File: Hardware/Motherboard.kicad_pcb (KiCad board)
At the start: 2 copper layers, 12 parts, among them J1 Conn_01x07_Male, U1 PIC18F23K22, U2 DS3231M, U3 Adafruit_BME680

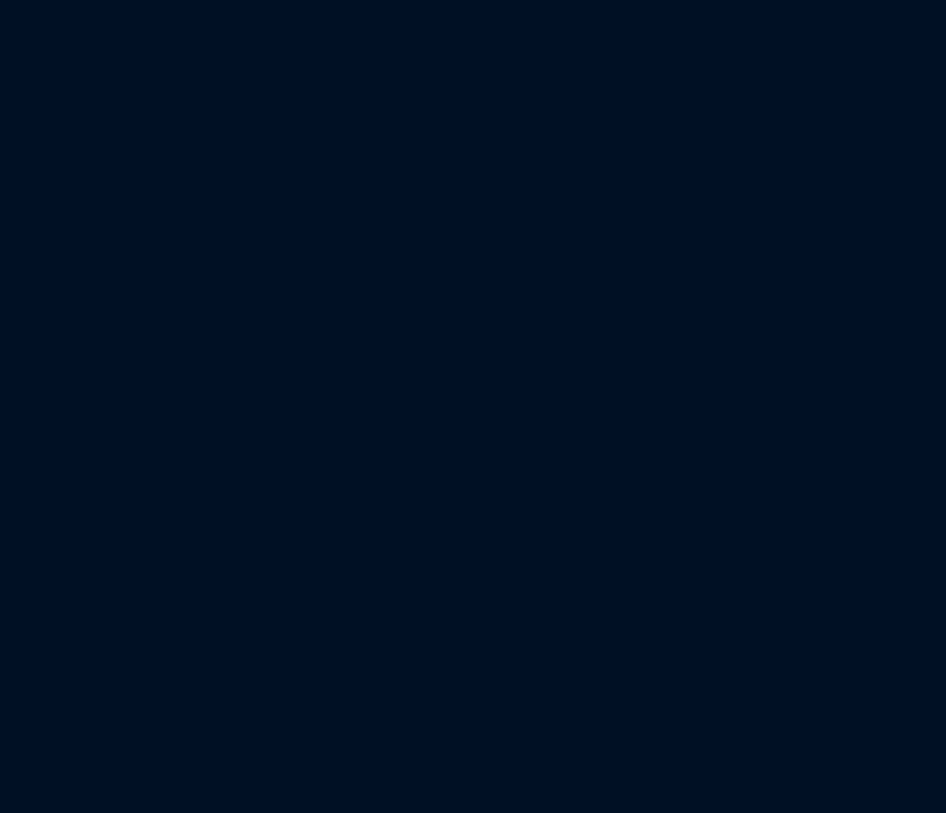
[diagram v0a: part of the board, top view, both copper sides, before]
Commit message: [Hardware] Replaced PIC18F26K22 microcontroller by PIC18F46K22 to have more pins.
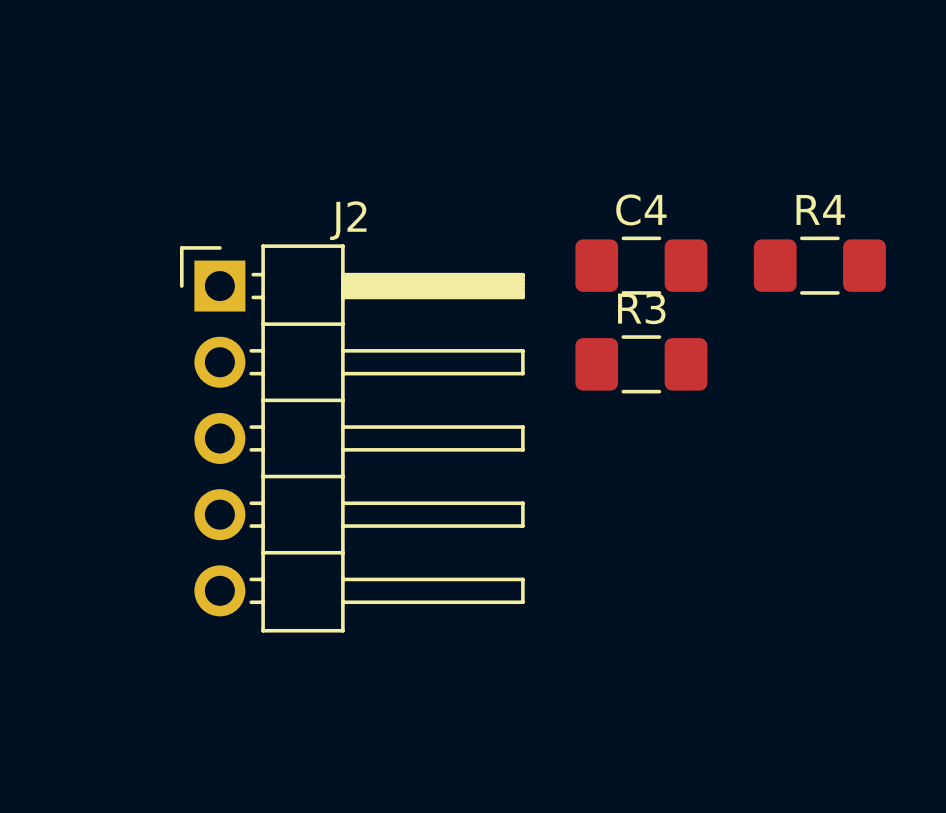
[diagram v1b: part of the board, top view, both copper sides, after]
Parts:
- added C4: 100n, Capacitor_SMD:C_1206_3216Metric_Pad1.42x1.75mm_HandSolder, F.Cu at (190.8, 23.4)
- added J2: Conn_01x05_Male, Connector_PinHeader_2.54mm:PinHeader_1x05_P2.54mm_Horizontal, F.Cu at (176.7, 24.0)
- added R3: 10K, Resistor_SMD:R_1206_3216Metric_Pad1.42x1.75mm_HandSolder, F.Cu at (190.8, 26.7)
- added R4: 220, Resistor_SMD:R_1206_3216Metric_Pad1.42x1.75mm_HandSolder, F.Cu at (196.7, 23.4)

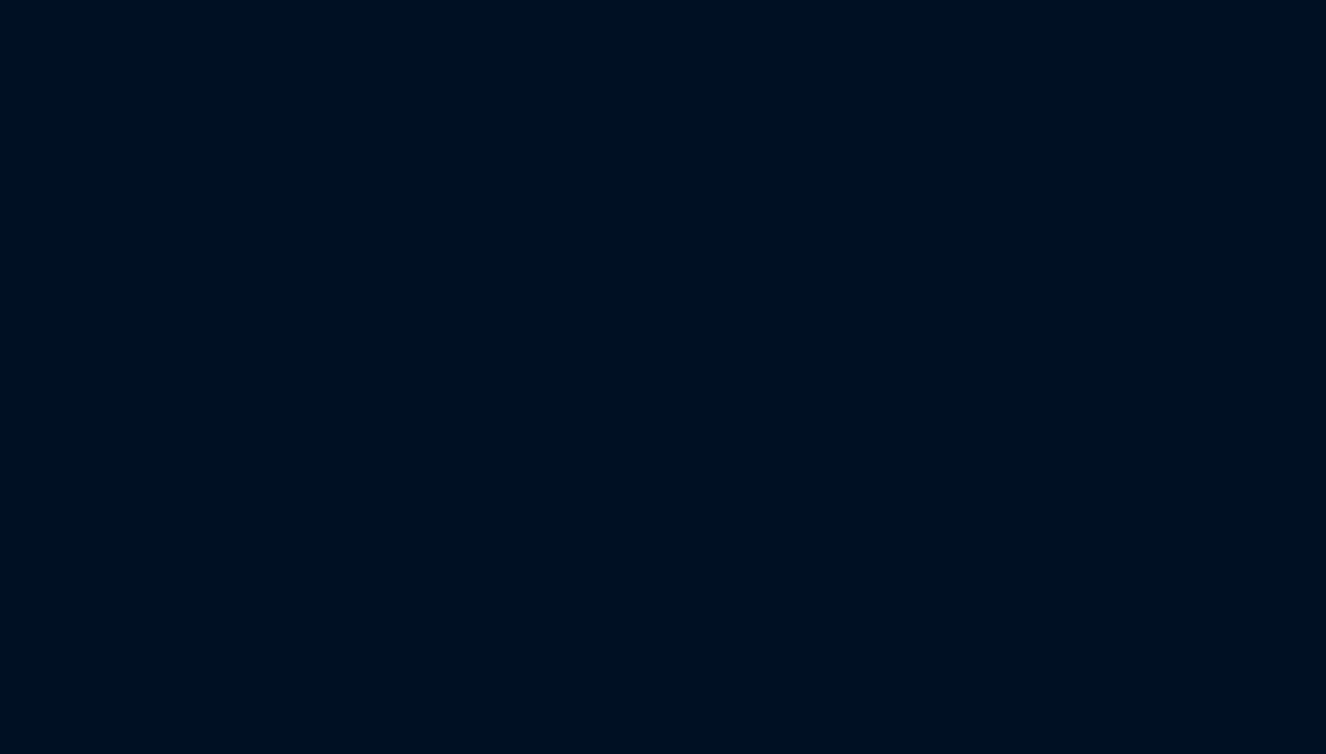
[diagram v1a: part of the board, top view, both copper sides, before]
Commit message: [Hardware] Added buttons.
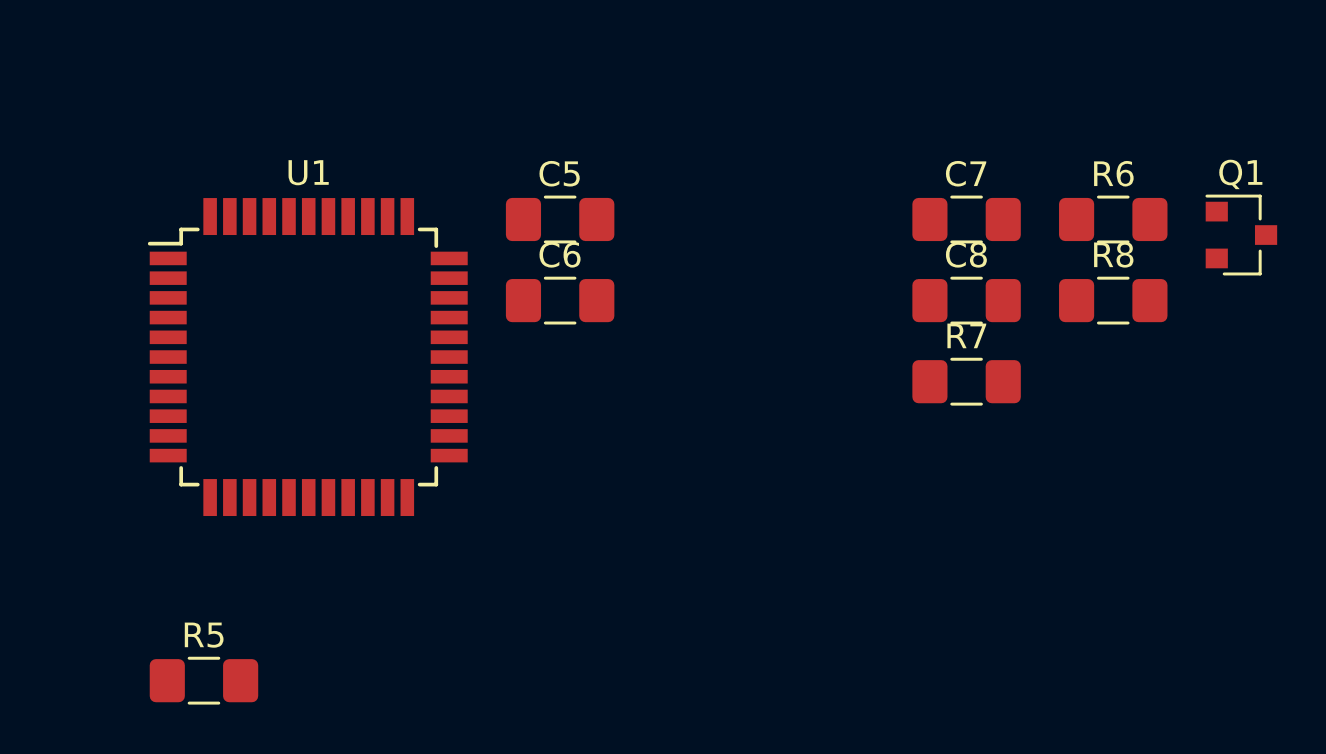
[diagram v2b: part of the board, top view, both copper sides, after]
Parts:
- added C5: 100n, Capacitor_SMD:C_1206_3216Metric_Pad1.42x1.75mm_HandSolder, F.Cu at (188.5, 74.2)
- added C6: 4.7u, Capacitor_SMD:C_1206_3216Metric_Pad1.42x1.75mm_HandSolder, F.Cu at (188.5, 77.5)
- added C7: 100n, Capacitor_SMD:C_1206_3216Metric_Pad1.42x1.75mm_HandSolder, F.Cu at (205.0, 74.2)
- added C8: 470n, Capacitor_SMD:C_1206_3216Metric_Pad1.42x1.75mm_HandSolder, F.Cu at (205.0, 77.5)
- added Q1: DMG3414U, Package_TO_SOT_SMD:SOT-23, F.Cu at (216.1, 74.8)
- added R5: 1K, Resistor_SMD:R_1206_3216Metric_Pad1.42x1.75mm_HandSolder, F.Cu at (174.0, 92.9)
- added R6: 12, Resistor_SMD:R_1206_3216Metric_Pad1.42x1.75mm_HandSolder, F.Cu at (210.9, 74.2)
- added R7: 12, Resistor_SMD:R_1206_3216Metric_Pad1.42x1.75mm_HandSolder, F.Cu at (205.0, 80.7)
- added R8: 1K, Resistor_SMD:R_1206_3216Metric_Pad1.42x1.75mm_HandSolder, F.Cu at (210.9, 77.5)
- added U1: PIC18F46K22-xPT, Package_QFP:TQFP-44_10x10mm_P0.8mm, F.Cu at (178.3, 79.7)
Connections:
- R4 pad 2: Net-(R4-Pad2) -> /RE3
- U2 pad 3: Net-(U2-Pad3) -> /Sensors_RTC/RTC_1HZ

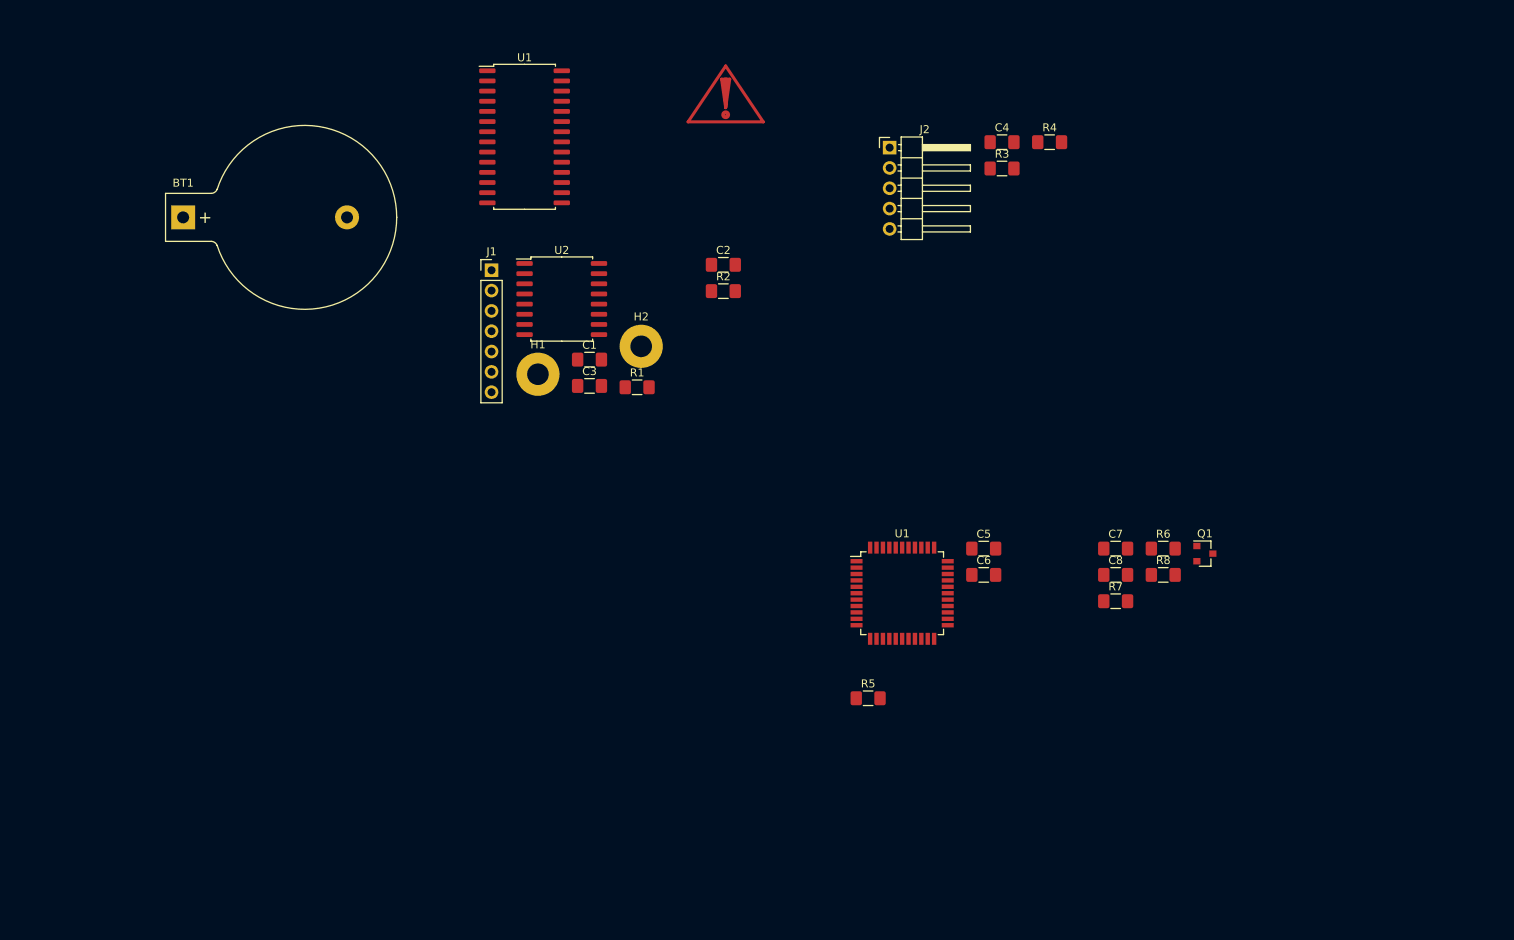
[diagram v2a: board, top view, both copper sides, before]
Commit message: [Hardware] Added all schematic parts (but not all external parts, like display or female connectors).
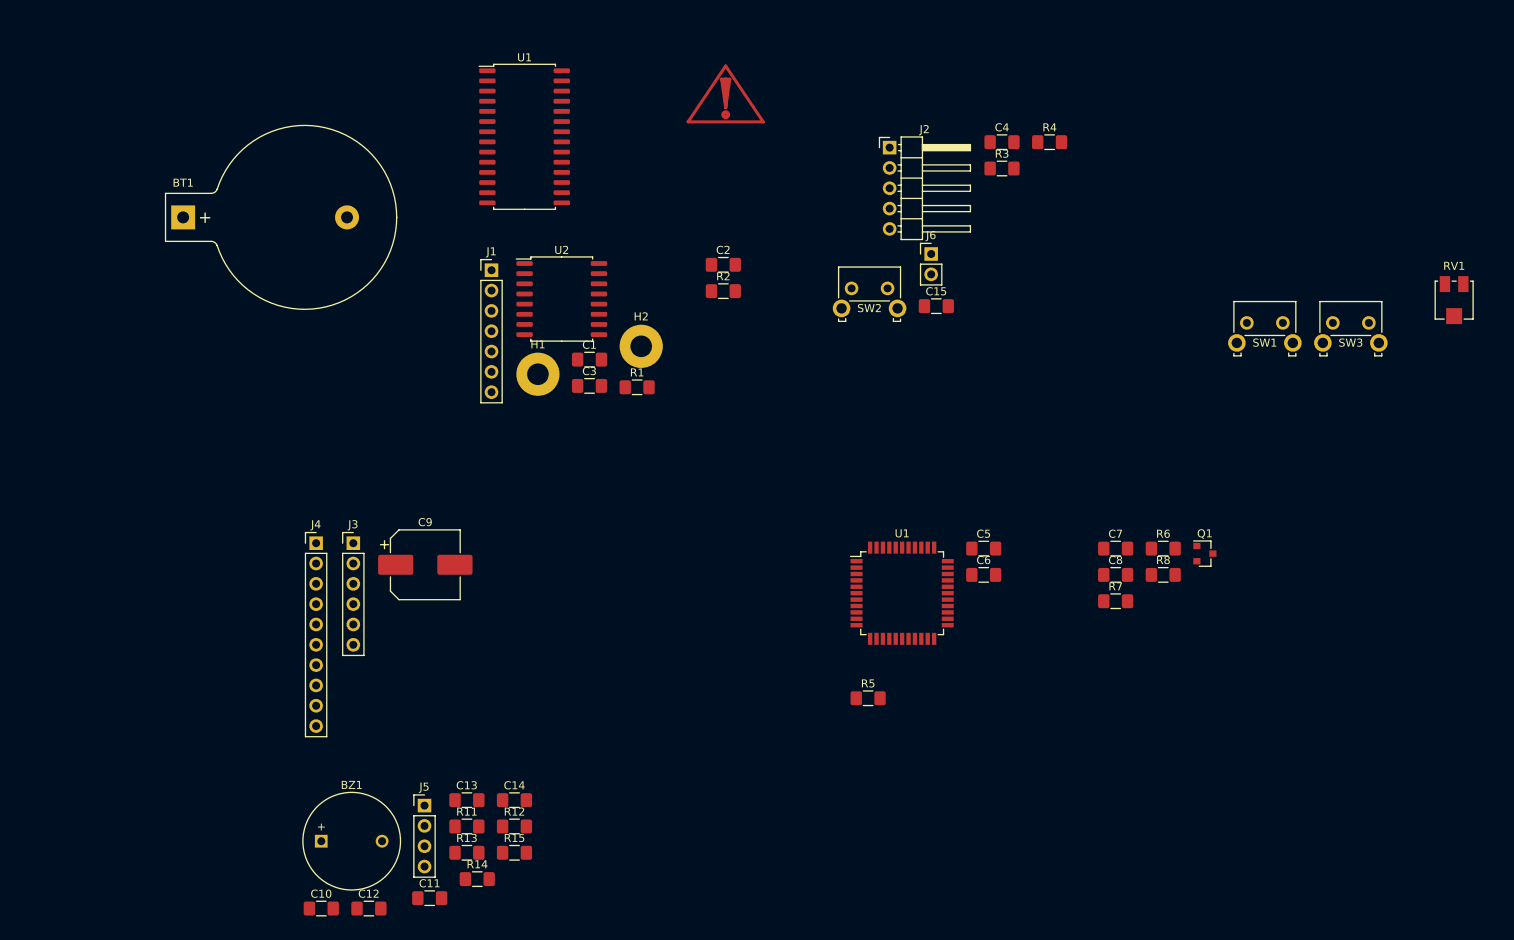
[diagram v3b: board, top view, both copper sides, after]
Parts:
- added BZ1: ABI-009-RC or SV12-5, Buzzer_Beeper:MagneticBuzzer_ProSignal_ABI-009-RC, F.Cu at (105.7, 110.7)
- added C10: 100n, Capacitor_SMD:C_1206_3216Metric_Pad1.42x1.75mm_HandSolder, F.Cu at (105.7, 119.2)
- added C11: 100n, Capacitor_SMD:C_1206_3216Metric_Pad1.42x1.75mm_HandSolder, F.Cu at (119.2, 117.9)
- added C12: 100n, Capacitor_SMD:C_1206_3216Metric_Pad1.42x1.75mm_HandSolder, F.Cu at (111.6, 119.2)
- added C13: 100n, Capacitor_SMD:C_1206_3216Metric_Pad1.42x1.75mm_HandSolder, F.Cu at (123.9, 105.6)
- added C14: 100n, Capacitor_SMD:C_1206_3216Metric_Pad1.42x1.75mm_HandSolder, F.Cu at (129.8, 105.6)
- added C15: 100n, Capacitor_SMD:C_1206_3216Metric_Pad1.42x1.75mm_HandSolder, F.Cu at (182.5, 43.9)
- added C9: 220u, Capacitor_SMD:CP_Elec_8x10.5, F.Cu at (118.7, 76.2)
- added J3: Conn_01x06_Male, Connector_PinHeader_2.54mm:PinHeader_1x06_P2.54mm_Vertical, F.Cu at (109.7, 73.5)
- added J4: Conn_01x10_Male, Connector_PinHeader_2.54mm:PinHeader_1x10_P2.54mm_Vertical, F.Cu at (105.0, 73.5)
- added J5: Conn_01x04_Male, Connector_PinHeader_2.54mm:PinHeader_1x04_P2.54mm_Vertical, F.Cu at (118.6, 106.3)
- added J6: Conn_01x02_Male, Connector_PinHeader_2.54mm:PinHeader_1x02_P2.54mm_Vertical, F.Cu at (181.9, 37.3)
- added R11: 10K, Resistor_SMD:R_1206_3216Metric_Pad1.42x1.75mm_HandSolder, F.Cu at (123.9, 108.9)
- added R12: 10K, Resistor_SMD:R_1206_3216Metric_Pad1.42x1.75mm_HandSolder, F.Cu at (129.8, 108.9)
- added R13: 10K, Resistor_SMD:R_1206_3216Metric_Pad1.42x1.75mm_HandSolder, F.Cu at (123.9, 112.2)
- added R14: 10K, Resistor_SMD:R_1206_3216Metric_Pad1.42x1.75mm_HandSolder, F.Cu at (125.2, 115.5)
- added R15: 10K, Resistor_SMD:R_1206_3216Metric_Pad1.42x1.75mm_HandSolder, F.Cu at (129.8, 112.2)
- added RV1: 10K, Potentiometer_SMD:Potentiometer_Bourns_3314J_Vertical, F.Cu at (247.3, 43.1)
- added SW1: SW_Push, Button_Switch_THT:SW_Tactile_SKHH_Angled, F.Cu at (221.4, 46.0)
- added SW2: SW_Push, Button_Switch_THT:SW_Tactile_SKHH_Angled, F.Cu at (171.9, 41.6)
- added SW3: SW_Push, Button_Switch_THT:SW_Tactile_SKHH_Angled, F.Cu at (232.1, 46.0)
- C8: value 470n -> 4.7u
- R8: value 1K -> 10K
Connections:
- U1 pad 10: Net-(U1-Pad10) -> /SETTINGS_BUTTON
- U1 pad 25: Net-(U1-Pad25) -> Net-(C11-Pad2)
- U1 pad 26: Net-(U1-Pad26) -> Net-(C10-Pad2)
- U1 pad 8: Net-(U1-Pad8) -> /ALARM_BUTTON
- U1 pad 9: Net-(U1-Pad9) -> /BACKLIGHT_BUTTON

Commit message: [Hardware] Started PCB routing. Components are placed, BME680 board mounting holes are in position, some nets are connected.
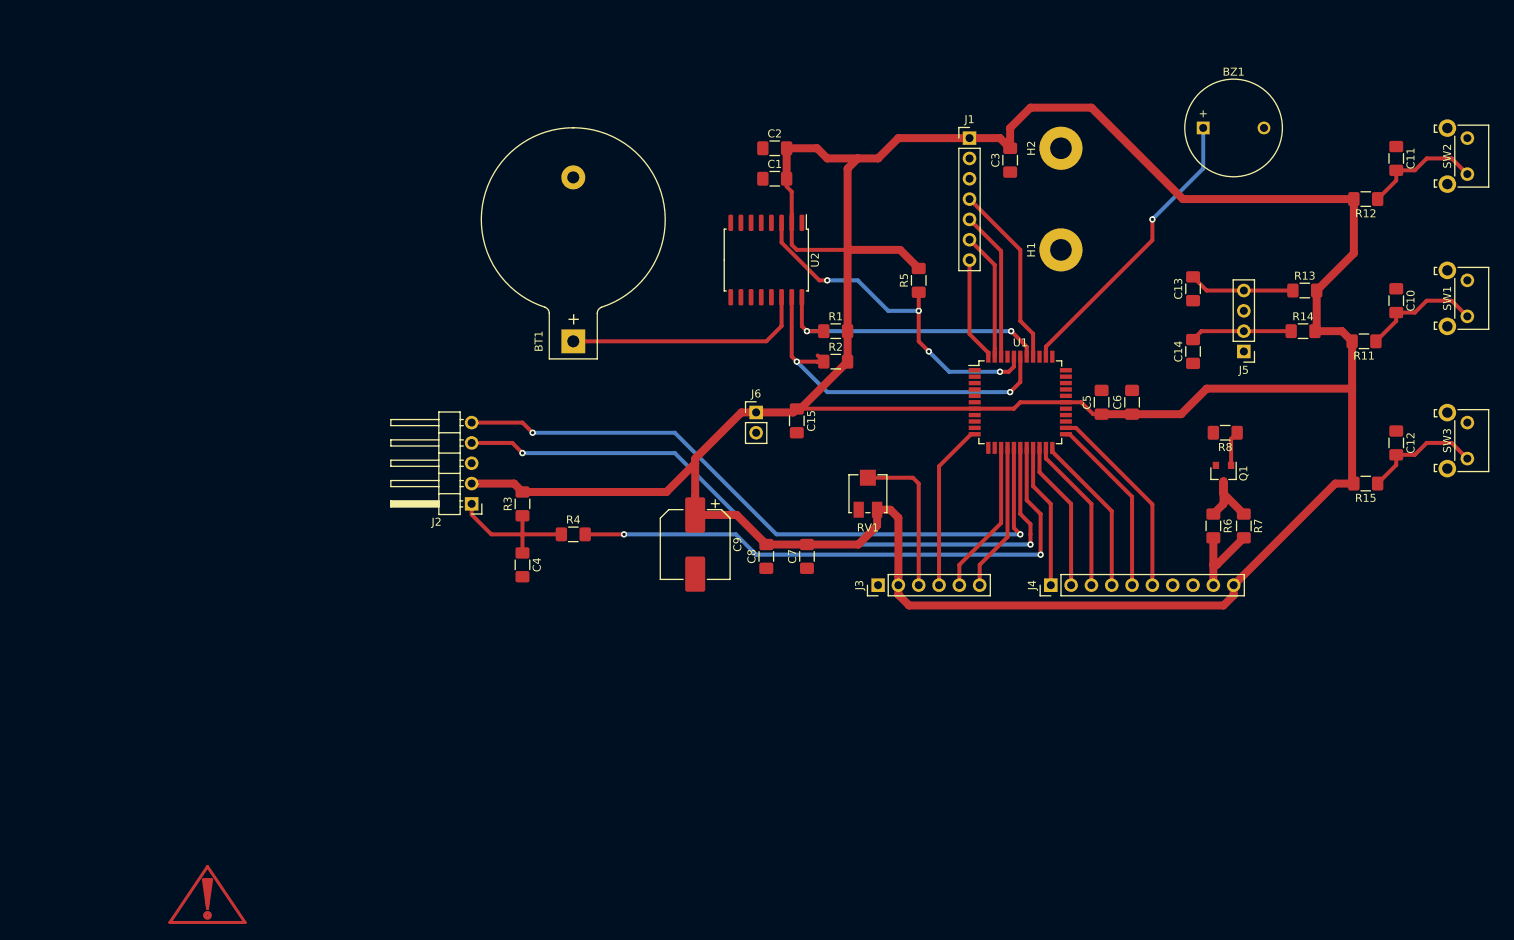
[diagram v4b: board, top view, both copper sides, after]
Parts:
- removed the U1 at (131.1, 22.7)
- J1: value Conn_01x07_Male -> BME680
- J3: value Conn_01x06_Male -> Display_1
- J4: value Conn_01x10_Male -> Display_2
- J5: value Conn_01x04_Male -> Buttons
- J6: value Conn_01x02_Male -> USB
- SW1: value SW_Push -> Button_Plus
- SW2: value SW_Push -> Button_Minus
- SW3: value SW_Push -> Button_Settings
- moved C10 154.4 mm to (240.0, 43.2), turned to 270 degrees
- moved C11 152.1 mm to (240.0, 25.4), turned to 270 degrees
- moved BZ1 141.8 mm to (215.9, 21.6)
- moved C12 141.0 mm to (240.0, 61.0), turned to 270 degrees
- moved R12 132.2 mm to (236.2, 30.5), turned to 180 degrees
- moved R11 127.5 mm to (236.0, 48.3), turned to 180 degrees
- moved R13 126.1 mm to (228.6, 41.9)
- moved R14 123.9 mm to (228.4, 47.0)
- moved U3 119.2 mm to (91.4, 118.1)
- moved J5 117.1 mm to (221.0, 49.5), turned to 180 degrees
- moved R15 116.0 mm to (236.2, 66.0), turned to 180 degrees
- moved C13 111.0 mm to (214.6, 41.7), turned to 90 degrees
- moved C14 101.7 mm to (214.6, 49.5), turned to 90 degrees
- moved J4 92.0 mm to (196.8, 78.7), turned to 90 degrees
- moved C4 79.9 mm to (130.8, 76.2), turned to 270 degrees
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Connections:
- SW3 pad 1: /SETTINGS_BUTTON -> GND
- SW3 pad 2: GND -> /SETTINGS_BUTTON
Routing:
- net +5V: track 0.00 -> 415.4 mm
- net Net-(J2-Pad4): track 0.00 -> 87.7 mm, vias 0 -> 2
- net Net-(J2-Pad5): track 0.00 -> 85.5 mm, vias 0 -> 2
- net /RE3: track 0.00 -> 72.1 mm, vias 0 -> 2
- net /Sensors_RTC/RTC_SDA: track 0.00 -> 46.0 mm, vias 0 -> 2
- net /Sensors_RTC/RTC_1HZ: track 0.00 -> 44.3 mm, vias 0 -> 4
- net Net-(BZ1-Pad1): track 0.00 -> 36.7 mm, vias 0 -> 1
- net /Sensors_RTC/RTC_SCL: track 0.00 -> 36.1 mm, vias 0 -> 2
- net Net-(BT1-Pad1): track 0.00 -> 30.4 mm
- net /Display/DISPLAY_DB5: track 0.00 -> 24.9 mm
- net /Sensors_RTC/BME680_SCK: track 0.00 -> 23.0 mm
- net /Display/DISPLAY_DB4: track 0.00 -> 22.6 mm
- net /Display/DISPLAY_RS: track 0.00 -> 21.0 mm
- net /Display/DISPLAY_DB3: track 0.00 -> 20.2 mm
- net /Display/DISPLAY_DB2: track 0.00 -> 19.5 mm
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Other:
- net class Default: trace_width 0.25 -> 0.5
- net class Power added: clearance 0.2, trace_width 1, via_dia 0.8, via_drill 0.4
